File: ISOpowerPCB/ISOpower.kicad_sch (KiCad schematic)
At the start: 10 parts

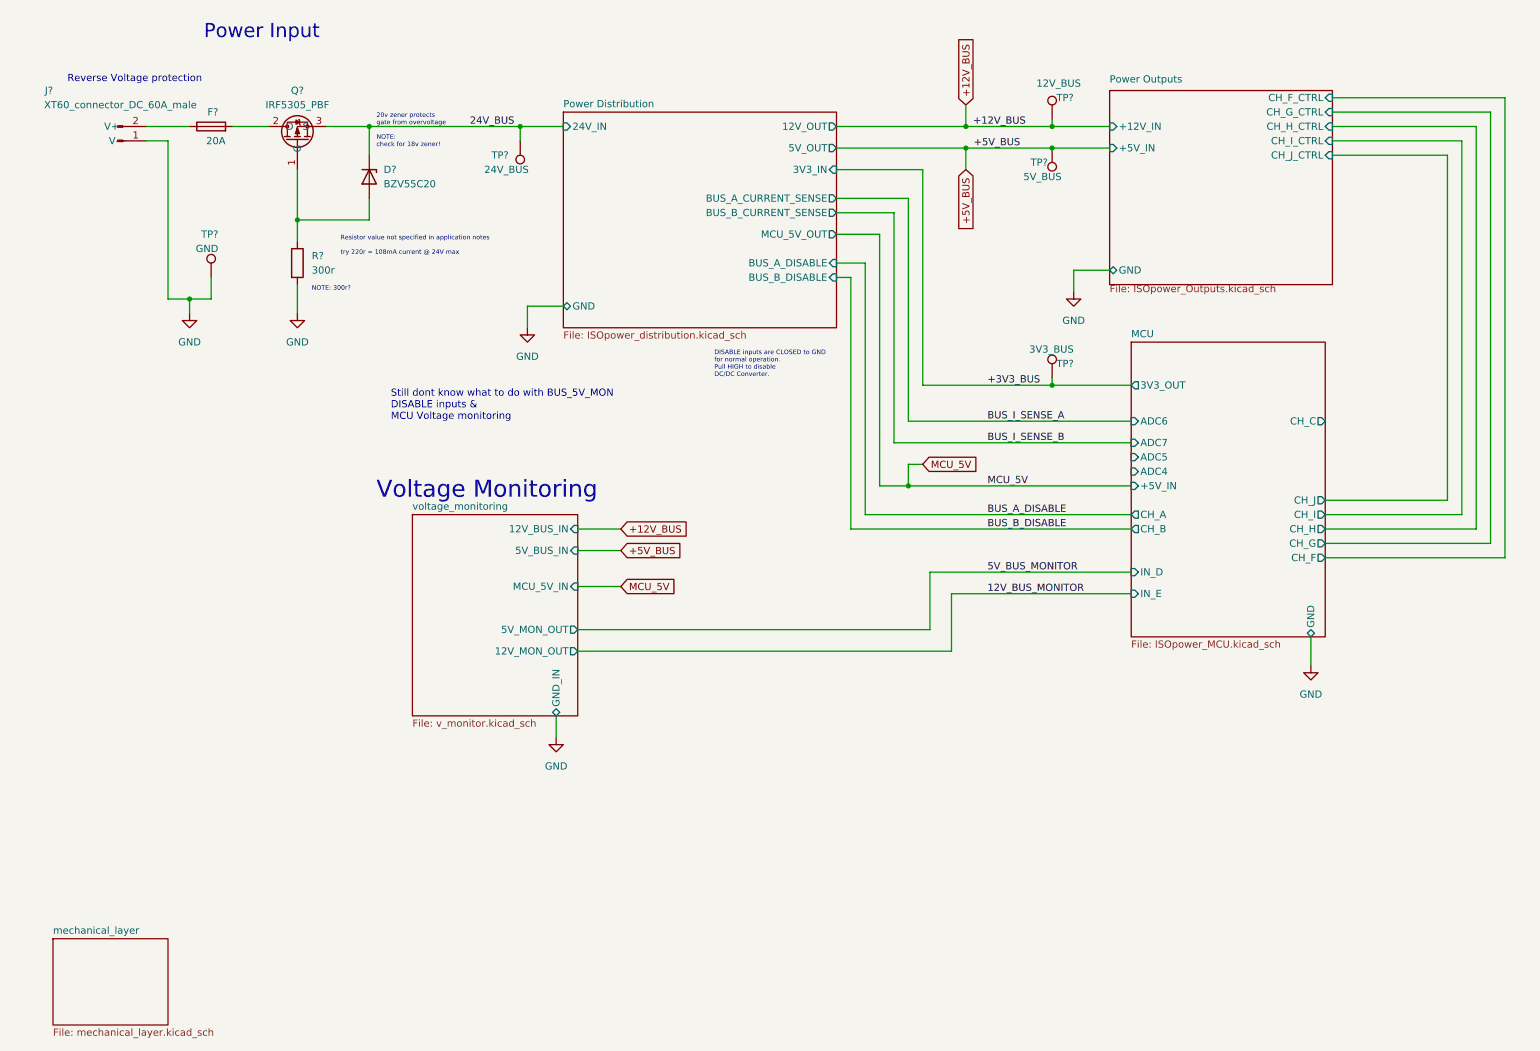
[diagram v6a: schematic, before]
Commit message: Updated as per discussions 26/01/22
# Change Notes

04/02/2022
As per discussion 26/01/22
1. Changed per channel 5v MOSFET switches to MOSFET control of DC/DC module on/off pin - due to failure of MOSFET switching during testing.
2. Added 5v buck converter for independent MCU_5V power bus.
	- Ensured all 5v MCU hardware is powered from common MCU_5V bus.
3. Removed circuit from NC pins on DC/DC modules.
4. Changed ESP32 USB interface to CH340
5. Changed MCU serial logic level converters from MOSFET to IC - TXS0102DCT
	- TODO: OE pin now requires low signal untill DC/DC supply is stable - Does it? Can it just be tied to 5v bus with a large capacitor? Does it need MCU to hold pin low untill 5V_BUS is stable?
6. Removed redundent 3V3_IN to power distribution page.
	- Rechecked all sheets for redundent pins, it won't impact drawing traces, but it will impact readability.
7. Added Mechanical layer as hirarchical sheet.
8. Moved voltage monitoring circuits to hirarchical sheet
9. Added voltage monitoring with TL431DBZ to 12V_BUS
10. Automatic shutoff circuit removed, as this would prevent the DC/DC module from powering on. Instead moved to AtMega328p digital inputs
and microcontroller will control shutdown of DC/DC supply if out of spec voltage detected.
		- This is a severe limitation compared to the specification, and this also does not prevent damage to devices on 5V_BUS if voltage is pulled high, for example to 12v due to user error.
		- TODO: Add independent overvoltage protection to 5V_BUS? 		[Zener Diode Overvoltage Protection - Sparkfun](https://www.rs-online.com/designspark/how-does-zener-diode-do-overvoltage-protection-in-circuit#:~:text=In%20order%20to%20protect%20the,flow%20in%20the%20reverse%20direction).
11. Changed logic level conversion for 12v outputs to 12v drive circuit. [12v drive circuit](https://forum.arduino.cc/t/easiest-way-of-driving-amplifying-from-5v-to-12v/123290)
12. Added proto pin connections for ESP MCU.
13. Changed 20v Zener in reverse vol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
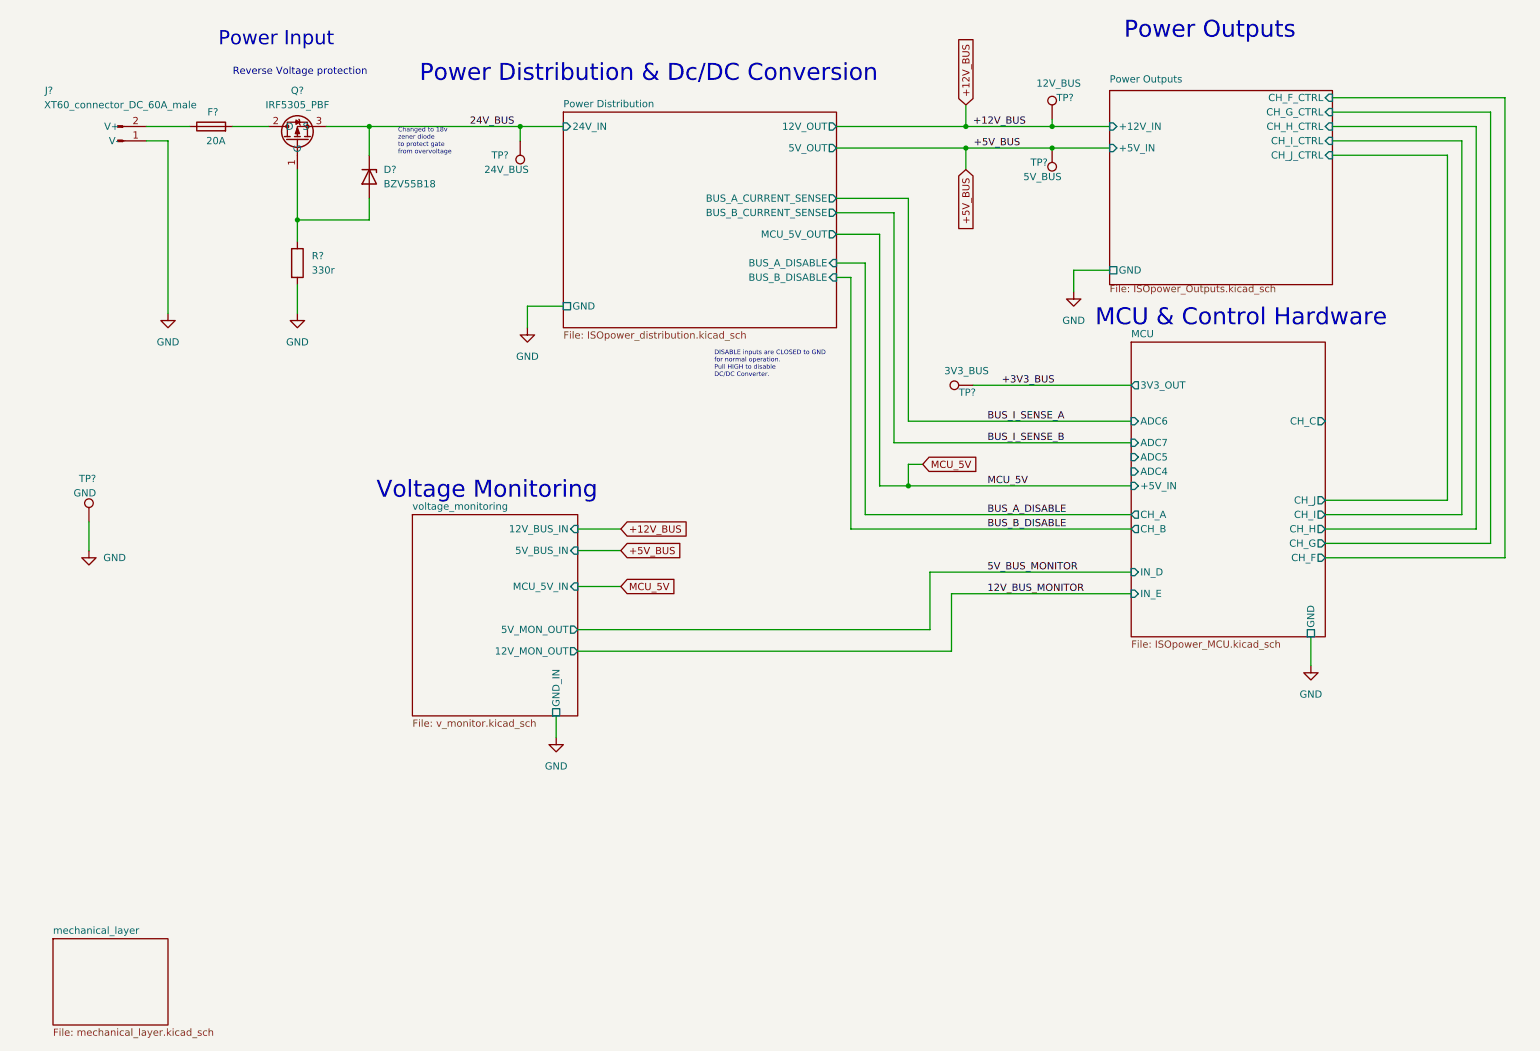
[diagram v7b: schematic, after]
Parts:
- removed D?: BZV55C20, Diode_SMD:D_MiniMELF, symbol Diode:BZV55C20
- added D?: BZV55B18, Diode_SMD:D_MiniMELF_Handsoldering, symbol Diode:BZV55B18
- R?: value 300r -> 330r
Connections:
- net 24V_BUS: now also D?.1 (K)
- net at Q?.1 (G), R?.1: now also D?.2 (A)
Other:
- sheet Power Distribution ports: added none; removed 3V3_IN
- note added: "Changed to 18v zener diode to protect gate from overvoltage"
- note added: "MCU & Control Hardware"
- note added: "Power Distribution & Dc/DC Conversion"
- note added: "Power Outputs"
- note removed: "20v zener protects gate from overvoltage NOTE: check for 18v zener!"
- note removed: "NOTE: 300r?"
- note removed: "Resistor value not specified in application notes try 220r = 108mA current @ 24V max"
- note removed: "Still dont know what to do with BUS_5V_MON DISABLE inputs & MCU Voltage monitoring"
- moved on the sheet: TP?

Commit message: messing around with libraries
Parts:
- gave numbers to parts that had none: 10
